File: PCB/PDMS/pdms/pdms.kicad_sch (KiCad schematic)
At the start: 46 parts, among them IC19 STM32L496ZGT6, IC20 AT25SF128A-SHB-T, J1 DBG, J2 6473427-1, Y1 48Mhz, Y2 32KHz

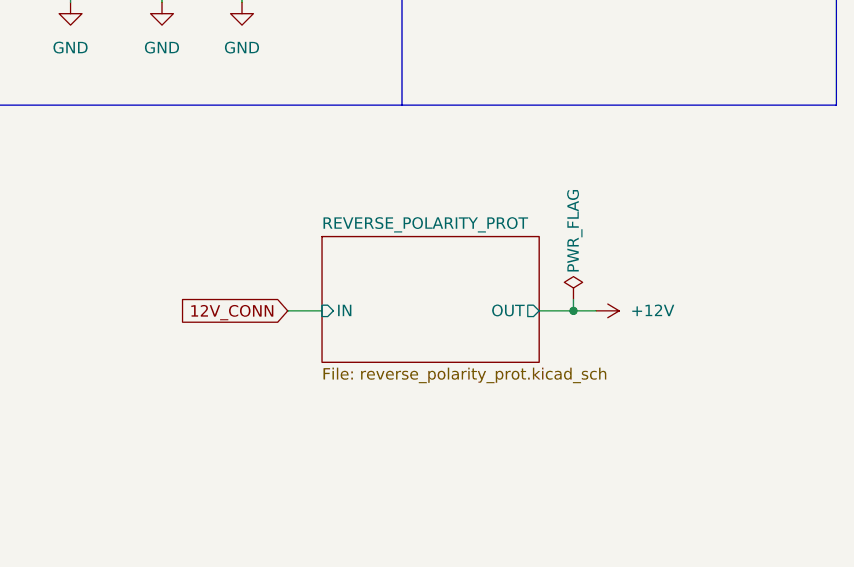
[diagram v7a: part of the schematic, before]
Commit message: Safety and led wiring
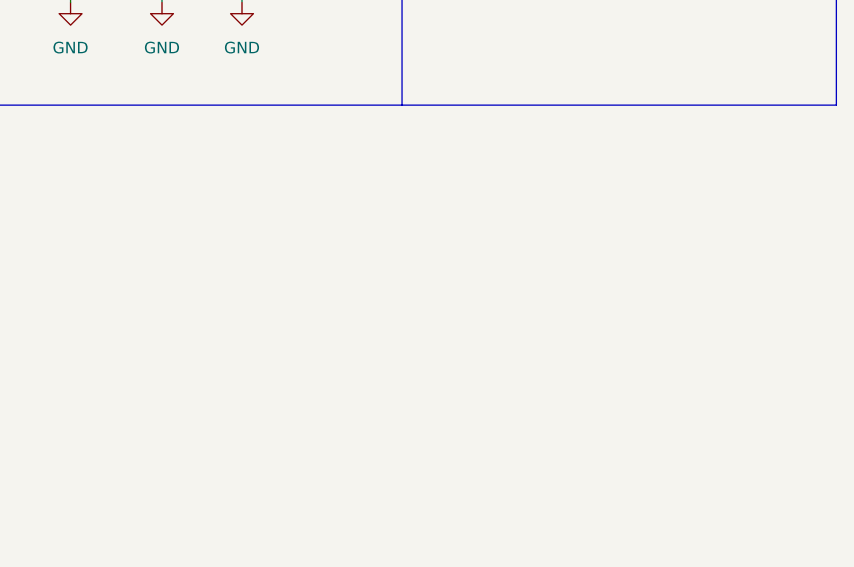
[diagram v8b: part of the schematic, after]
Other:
- removed sheet REVERSE_POLARITY_PROT
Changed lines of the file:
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@@
   (bus_alias "QUADSPI" (members "CLK" "NCS" "BK1_IO0" "BK1_IO1" "BK1_IO2" "BK1_IO3"))
   (bus_alias "SPI3" (members "SCK" "MOSI" "MISO"))
-  (bus_alias "SPI2" (members "SCK" "MISO" "MOSI"))
   (bus_alias "SPI1" (members "SCK" "MOSI" "MISO"))
+  (bus_alias "SPI2" (members "SCK" "MISO" "MOSI"))
   (junction (at 262.89 106.68) (diameter 0) (color 0 0 0 0)
   )
@@
   (junction (at 228.6 50.8) (diameter 0) (color 0 0 0 0)
   )
-  (junction (at 378.46 147.32) (diameter 0) (color 0 0 0 0)
-  )
   (junction (at 245.11 116.84) (diameter 0) (color 0 0 0 0)
   )
@@
     (stroke (width 0) (type default) (color 0 0 0 0))
   )
-  (wire (pts (xy 346.71 147.32) (xy 350.52 147.32))
-    (stroke (width 0) (type default) (color 0 0 0 0))
-  )
   (bus (pts (xy 191.77 168.91) (xy 191.77 171.45))
     (stroke (width 0) (type default) (color 0 0 0 0))
@@
     (stroke (width 0) (type default) (color 0 0 0 0))
   )
-  (wire (pts (xy 378.46 146.05) (xy 378.46 147.32))
-    (stroke (width 0) (type default) (color 0 0 0 0))
-  )
   (wire (pts (xy 271.78 106.68) (xy 280.67 106.68))
     (stroke (width 0) (type default) (color 0 0 0 0))
@@
     (stroke (width 0) (type default) (color 0 0 0 0))
   )
-  (wire (pts (xy 374.65 147.32) (xy 378.46 147.32))
-    (stroke (width 0) (type default) (color 0 0 0 0))
-  )
   (wire (pts (xy 26.035 119.38) (xy 26.035 111.76))
     (stroke (width 0) (type default) (color 0 0 0 0))
@@
     (stroke (width 0) (type default) (color 0 0 0 0))
   )
-  (wire (pts (xy 378.46 147.32) (xy 381 147.32))
-    (stroke (width 0) (type default) (color 0 0 0 0))
-  )
   (wire (pts (xy 260.35 134.62) (xy 260.35 132.08))
     (stroke (width 0) (type default) (color 0 0 0 0))
@@
     )
   )
-  (global_label "12V_CONN" (shape input) (at 346.71 147.32 180) (fields_autoplaced)
-    (effects (font (size 1.27 1.27)) (justify right))
-    (property "Intersheet References" "${INTERSHEET_REFS}" (id 0) (at 334.5602 147.2406 0)
-      (effects (font (size 1.27 1.27)) (justify right) hide)
-    )
-  )
   (global_label "HP_MOS3" (shape input) (at 139.065 334.645 0) (fields_autoplaced)
     (effects (font (size 1.27 1.27)) (justify left))
@@
     (pin "1")
   )
-  (symbol (lib_id "power:PWR_FLAG") (at 378.46 146.05 0) (unit 1)
-    (in_bom yes) (on_board yes)
-    (property "Reference" "#FLG0105" (id 0) (at 378.46 144.145 0)
-      (effects (font (size 1.27 1.27)) hide)
-    )
-    (property "Value" "PWR_FLAG" (id 1) (at 378.46 138.43 90))
-    (property "Footprint" "" (id 2) (at 378.46 146.05 0)
-      (effects (font (size 1.27 1.27)) hide)
-    )
-    (property "Datasheet" "~" (id 3) (at 378.46 146.05 0)
-      (effects (font (size 1.27 1.27)) hide)
-    )
-    (pin "1")
-  )
   (symbol (lib_id "Device:C_Small") (at 280.67 137.16 0) (unit 1)
     (in_bom yes) (on_board yes)
@@
     (pin "2")
   )
-  (symbol (lib_id "power:+12V") (at 381 147.32 270) (unit 1)
-    (in_bom yes) (on_board yes) (fields_autoplaced)
-    (property "Reference" "#PWR0252" (id 0) (at 377.19 147.32 0)
-      (effects (font (size 1.27 1.27)) hide)
-    )
-    (property "Value" "+12V" (id 1) (at 384.81 147.3199 90)
-      (effects (font (size 1.27 1.27)) (justify left))
-    )
-    (property "Footprint" "" (id 2) (at 381 147.32 0)
-      (effects (font (size 1.27 1.27)) hide)
-    )
-    (property "Datasheet" "" (id 3) (at 381 147.32 0)
-      (effects (font (size 1.27 1.27)) hide)
-    )
-    (pin "1")
-  )
   (symbol (lib_id "Device:C_Small") (at 234.95 114.3 0) (unit 1)
     (in_bom yes) (on_board yes)
@@
     )
   )
-  (sheet (at 350.52 139.065) (size 24.13 13.97) (fields_autoplaced)
-    (stroke (width 0.1524) (type solid) (color 0 0 0 0))
-    (fill (color 0 0 0 0.0000))
-    (property "Sheet name" "REVERSE_POLARITY_PROT" (id 0) (at 350.52 138.3534 0)
-      (effects (font (size 1.27 1.27)) (justify left bottom))
-    )
-    (property "Sheet file" "reverse_polarity_prot.kicad_sch" (id 1) (at 350.52 153.6196 0)
-      (effects (font (size 1.27 1.27)) (justify left top))
-    )
-    (pin "IN" input (at 350.52 147.32 180)
-      (effects (font (size 1.27 1.27)) (justify left))
-    )
-    (pin "OUT" output (at 374.65 147.32 0)
-      (effects (font (size 1.27 1.27)) (justify right))
-    )
-  )
   (sheet (at 24.13 128.905) (size 20.32 14.605) (fields_autoplaced)
     (stroke (width 0.1524) (type solid) (color 0 0 0 0))
@@
     (path "/" (page "1"))
     (path "/0bc730b5-3de0-4ee2-82e7-e6324d6cb059" (page "15"))
-    (path "/38112cda-c962-4efc-8abd-7fa61cf21a14" (page "15"))
     (path "/ede01c72-e1bf-446e-aa54-1b058e72b3c5" (page "16"))
     (path "/2d272d29-2d37-453d-ba8c-6739a3d9a27c" (page "16"))
@@
       (reference "#FLG0104") (unit 1) (value "PWR_FLAG") (footprint "")
     )
-    (path "/806b4ec5-d53f-42a2-a20b-1ce786696c8d"
-      (reference "#FLG0105") (unit 1) (value "PWR_FLAG") (footprint "")
-    )
     (path "/72233c42-cc52-48f1-96b2-587884f89204/626922b0-20ac-4c03-97d3-4ca03f9f7909"
       (reference "#PWR0193") (unit 1) (value "GND") (footprint "")
@@
       (reference "#PWR0248") (unit 1) (value "GND") (footprint "")
     )
-    (path "/38112cda-c962-4efc-8abd-7fa61cf21a14/44e86f6b-de50-4f2a-8244-76cfd3c30567"
-      (reference "#PWR0249") (unit 1) (value "GND") (footprint "")
-    )
-    (path "/38112cda-c962-4efc-8abd-7fa61cf21a14/e797e1e4-2539-4d95-98ba-c2050748e265"
-      (reference "#PWR0250") (unit 1) (value "GND") (footprint "")
-    )
-    (path "/38112cda-c962-4efc-8abd-7fa61cf21a14/a58d0c52-03b4-4d81-9a30-a480684e53dc"
-      (reference "#PWR0251") (unit 1) (value "GND") (footprint "")
-    )
-    (path "/c4911646-a5c5-4ff0-b51d-631472b66f87"
-      (reference "#PWR0252") (unit 1) (value "+12V") (footprint "")
-    )
     (path "/2d272d29-2d37-453d-ba8c-6739a3d9a27c/cefab86a-00ed-405d-86c4-08a82a6dd03b"
       (reference "#PWR0253") (unit 1) (value "+3.3V") (footprint "")
@@
       (reference "#PWR0326") (unit 1) (value "+5V") (footprint "")
     )
-    (path "/5e0d1f91-4fae-411e-a2b8-95f4b4fcadc5/ca584d03-cfff-4b69-be36-20e3f4b62f16"
-      (reference "#PWR0327") (unit 1) (value "+5V") (footprint "")
-    )
     (path "/5e0d1f91-4fae-411e-a2b8-95f4b4fcadc5/486623ed-73ea-4ef8-9309-d89051c5d677"
       (reference "#PWR0328") (unit 1) (value "GND") (footprint "")
@@
       (reference "#PWR0332") (unit 1) (value "GND") (footprint "")
     )
-    (path "/5e0d1f91-4fae-411e-a2b8-95f4b4fcadc5/848a5e0d-f7f9-4954-adc6-b7de70f4191b"
-      (reference "#PWR0333") (unit 1) (value "+5V") (footprint "")
-    )
-    (path "/5e0d1f91-4fae-411e-a2b8-95f4b4fcadc5/61c4d3d9-07ae-4ba6-b0ea-d63fd6015400"
-      (reference "#PWR0334") (unit 1) (value "+5V") (footprint "")
-    )
-    (path "/5e0d1f91-4fae-411e-a2b8-95f4b4fcadc5/ce621144-5a3e-4398-aae4-62418250a692"
-      (reference "#PWR0335") (unit 1) (value "+5V") (footprint "")
-    )
-    (path "/5e0d1f91-4fae-411e-a2b8-95f4b4fcadc5/4e6b37e5-7393-476a-af95-c6a2eebb8d93"
-      (reference "#PWR0336") (unit 1) (value "+5V") (footprint "")
-    )
-    (path "/5e0d1f91-4fae-411e-a2b8-95f4b4fcadc5/e9601495-68ca-4b86-a7eb-98975f1250e3"
-      (reference "#PWR0337") (unit 1) (value "+5V") (footprint "")
-    )
-    (path "/5e0d1f91-4fae-411e-a2b8-95f4b4fcadc5/64f3aa0a-09f8-4ca4-bb8a-92d7815038b4"
-      (reference "#PWR0338") (unit 1) (value "+5V") (footprint "")
-    )
     (path "/5e0d1f91-4fae-411e-a2b8-95f4b4fcadc5/5fb10aca-38e1-4b89-8b8c-d0125c852a56"
       (reference "#PWR0339") (unit 1) (value "GND") (footprint "")
@@
       (reference "#PWR0340") (unit 1) (value "GND") (footprint "")
     )
-    (path "/5e0d1f91-4fae-411e-a2b8-95f4b4fcadc5/5617de9c-1a54-49c8-bf32-1a5f3128826e"
-      (reference "#PWR0341") (unit 1) (value "+5V") (footprint "")
-    )
     (path "/5e0d1f91-4fae-411e-a2b8-95f4b4fcadc5/171034fd-c0d6-44a2-9b05-58005e268432"
       (reference "#PWR0342") (unit 1) (value "GND") (footprint "")
@@
       (reference "C63") (unit 1) (value "22uF") (footprint "Resistor_SMD:R_0402_1005Metric")
     )
-    (path "/38112cda-c962-4efc-8abd-7fa61cf21a14/516e33b3-5bfc-4b38-88de-fa9fccbda6e5"
-      (reference "C64") (unit 1) (value "22uF") (footprint "Capacitor_SMD:C_0805_2012Metric")
-    )
-    (path "/38112cda-c962-4efc-8abd-7fa61cf21a14/8c8fda44-63a2-48ec-85ff-df1634fbb0ba"
-      (reference "C65") (unit 1) (value "0.1uF") (footprint "Resistor_SMD:R_0402_1005Metric")
-    )
-    (path "/38112cda-c962-4efc-8abd-7fa61cf21a14/8491d2d4-8b2c-4b93-b5ac-1edd327852d7"
-      (reference "C66") (unit 1) (value "100nF") (footprint "Capacitor_SMD:C_0805_2012Metric")
-    )
     (path "/f973e110-c9eb-4494-a7eb-37628bac99f8/808924b7-27d2-4209-a500-7d9830d3c986"
       (reference "C74") (unit 1) (value "100nF") (footprint "Capacitor_SMD:C_0402_1005Metric_Pad0.74x0.62mm_HandSolder")
@@
       (reference "IC14") (unit 1) (value "TMP126NDCKR") (footprint "PDM_Additional:SOT65P210X110-6N")
     )
-    (path "/38112cda-c962-4efc-8abd-7fa61cf21a14/fca9331b-b9ba-4fc8-a2ac-16178519212a"
-      (reference "IC15") (unit 1) (value "LM74700MDDFREP") (footprint "PDMS_Additional:SOT65P280X110-8N")
-    )
     (path "/f973e110-c9eb-4494-a7eb-37628bac99f8/5a63e430-8662-4495-a1a8-64838f3132cd"
       (reference "IC17") (unit 1) (value "ASM330LHHTR") (footprint "PDMS_Additional:LGA-14_2.5X3X0.86_")
@@
       (reference "Q2") (unit 1) (value "MMBT3904") (footprint "Package_TO_SOT_SMD:SOT-23")
     )
-    (path "/38112cda-c962-4efc-8abd-7fa61cf21a14/ed159608-e404-4209-af0c-d2be60349f3e"
-      (reference "Q3") (unit 1) (value "IAUA250N04S6N007AUMA1") (footprint "PDM_Additional:IAUA250N04S6N007AUMA1")
-    )
     (path "/c95687f0-d188-4c79-a818-a8c3947d28e2"
